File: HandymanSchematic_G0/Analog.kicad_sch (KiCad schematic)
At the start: 60 parts, among them Q1 BC847, Q2 BC847, U1 TL074, U2 TL074, U3 TL072

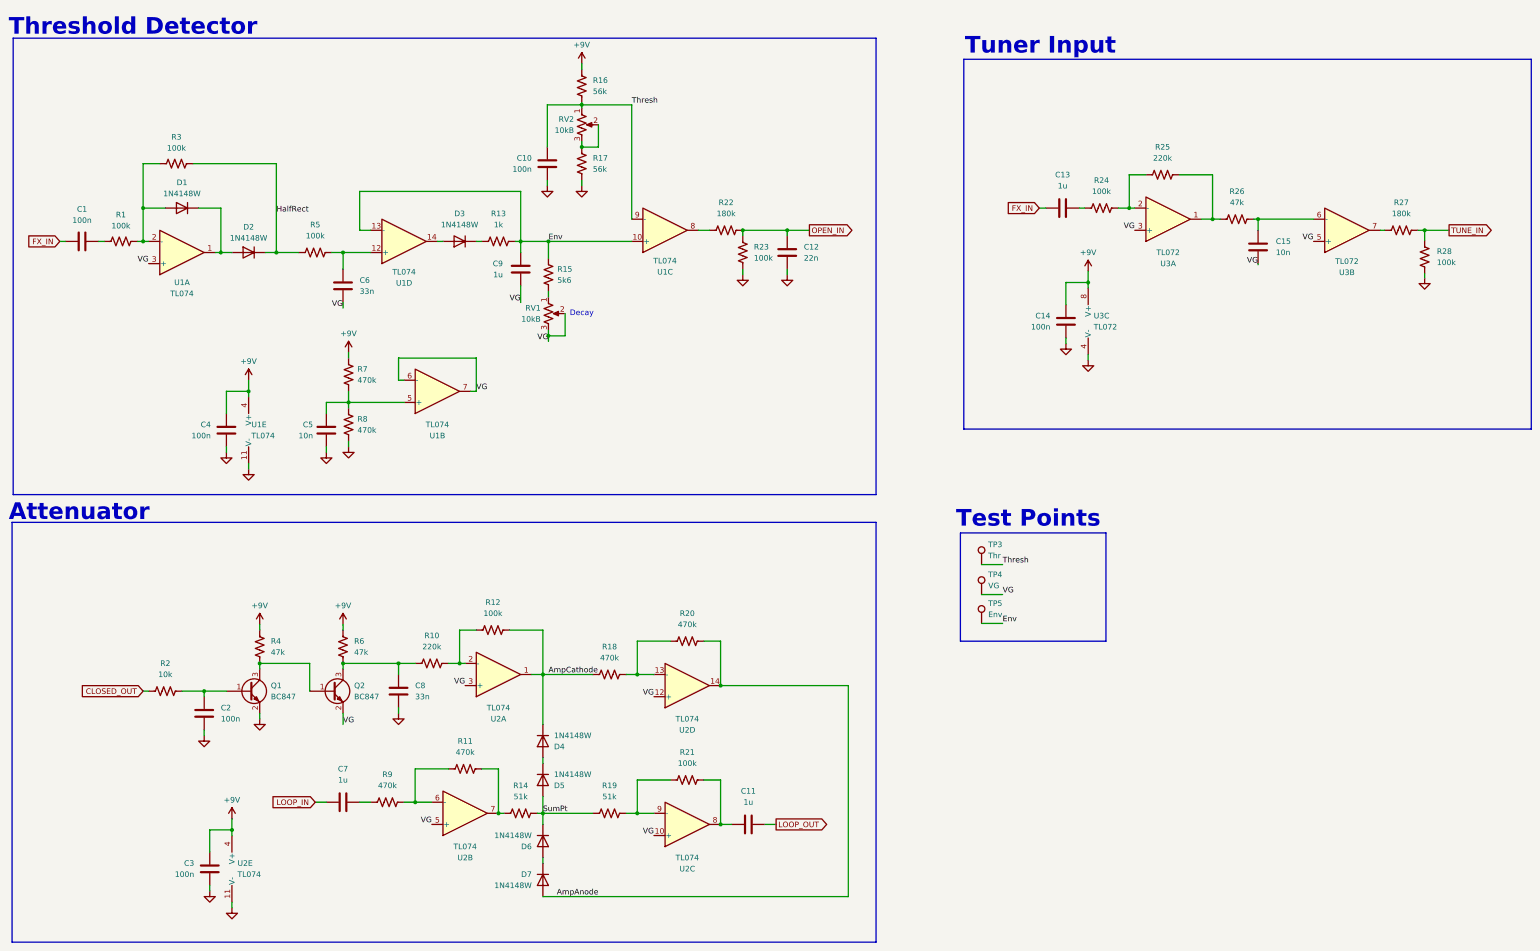
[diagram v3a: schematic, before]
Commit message: analog tweaks, 2 fewer op amps
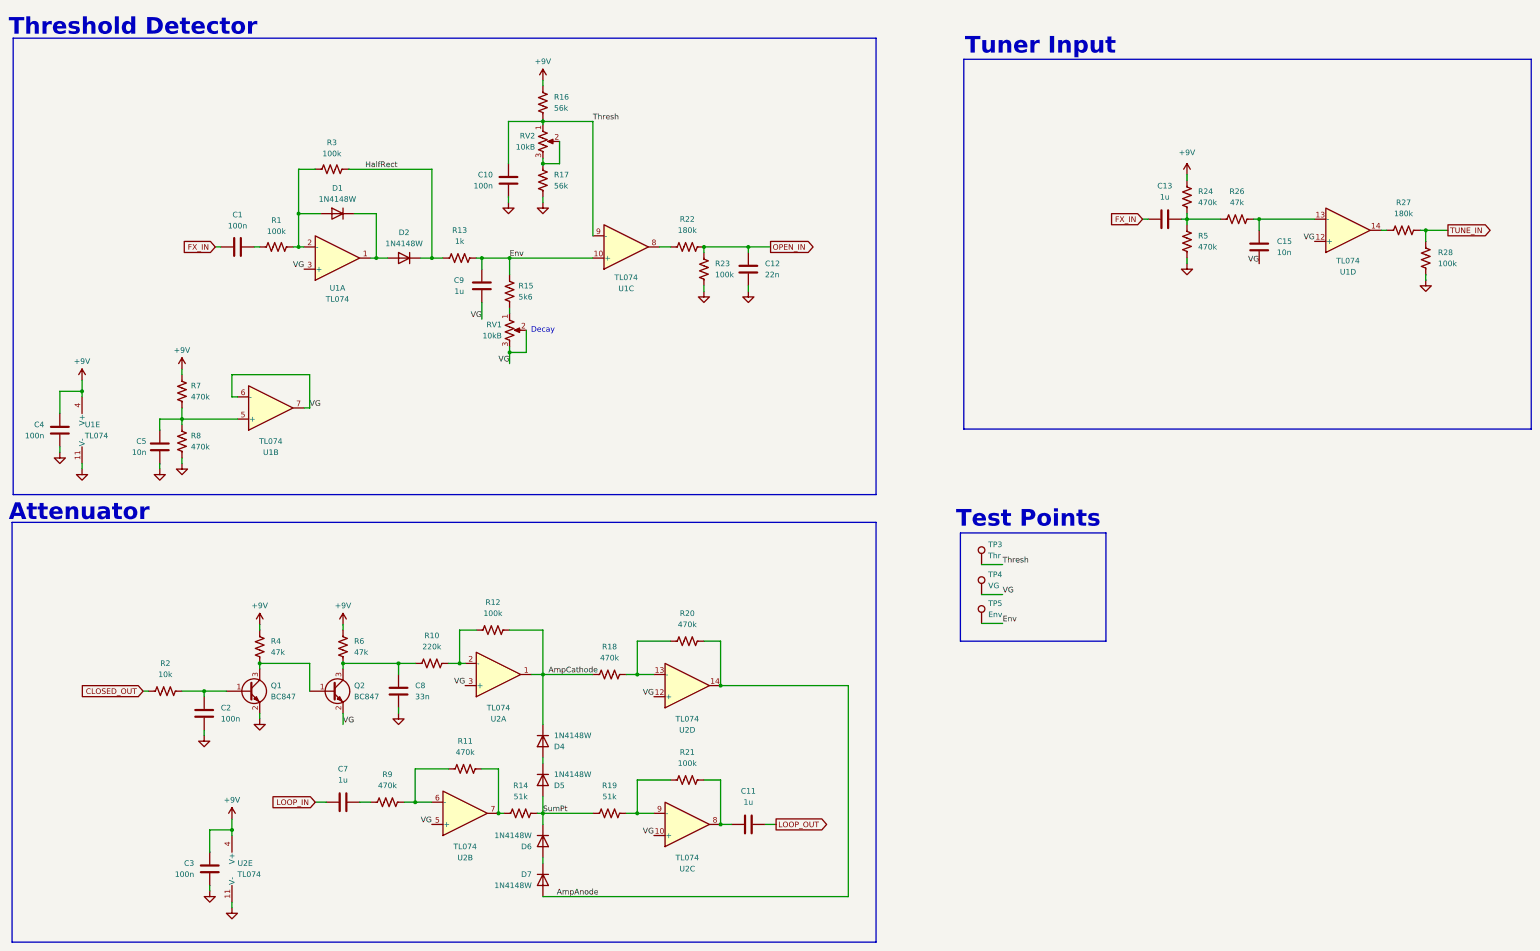
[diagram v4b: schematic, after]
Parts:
- removed C14: 100n, Capacitor_SMD:C_0805_2012Metric, symbol Device:C
- removed C6: 33n, Capacitor_SMD:C_0805_2012Metric, symbol Device:C
- removed D3: 1N4148W, Diode_SMD:D_SOD-123, symbol Diode:1N4148W
- removed R25: 220k, Resistor_SMD:R_0805_2012Metric, symbol Device:R_US
- removed U3: TL072, Package_SO:SOIC-8_3.9x4.9mm_P1.27mm, symbol Amplifier_Operational:TL072
- R24, R5: value 100k -> 470k
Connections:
- net +9V: now also R24.2
- net Env: no longer U1.13 (-)
- net GND: now also R5.1
- net HalfRect: now also R13.1; no longer R5.1
- net VG: now also U1.12 (+)
- net at U1.14: now also R27.1
- net at R5.2: now also C13.2, R24.1, R26.1; no longer U1.12 (+)
- net at C15.2, R26.2: now also U1.13 (-)
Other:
- moved on the sheet: C1, C10, C12, C13, C4, C5, C9, D1, D2, R1, R13, R15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

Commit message: simplified attenuator input stage
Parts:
- removed C8: 33n, Capacitor_SMD:C_0805_2012Metric, symbol Device:C
- removed Q2: BC847, Package_TO_SOT_SMD:SOT-23, symbol Transistor_BJT:BC847
- removed R6: 47k, Resistor_SMD:R_0805_2012Metric, symbol Device:R_US
- added D201: 1N4148W, Diode_SMD:D_SOD-123, symbol Diode:1N4148W
- added R201: 47k, Resistor_SMD:R_0805_2012Metric, symbol Device:R_US
- added R202: 100k, Resistor_SMD:R_0805_2012Metric, symbol Device:R_US
- R10: value 220k -> 47k
- R12: value 100k -> 470k
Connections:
- net VG: now also R202.2
- net at Q1.3 (C), R4.2: now also D201.2 (A)
- net at R10.1: now also R201.2, R202.1
- new net: D201.1 (K), R201.1
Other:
- moved on the sheet: C2, Q1, R2, R4

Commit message: prelim layout
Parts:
- removed TP4: VG, TestPoint:TestPoint_THTPad_D2.0mm_Drill1.0mm_VAL, symbol Connector:TestPoint
- renumbered C4 to C1, C11 to C10, C13 to C11, C15 to C12, C5 to C2, C2 to C4, C1 to C5, C7 to C6, C9 to C7, C10 to C8, C12 to C9, D201 to D1, D1 to D2, D2 to D3, R7 to R1, R13 to R11, R11 to R12, R12 to R13, R15 to R14, R14 to R15, R8 to R2, R22 to R20, R20 to R21, R21 to R22, R5 to R25, R2 to R3, R1 to R4, R4 to R5, R3 to R6, R201 to R7, R9 to R8, R202 to R9, TP3 to TP1, TP5 to TP3
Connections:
- net AmpAnode: now also U2.7; no longer U2.14
- net Env: now also U1.12 (+); no longer U1.10 (+)
- net Thresh: now also U1.13 (-); no longer U1.9 (-)
- net VG: now also U1.10 (+); no longer U1.12 (+)
- net at U1.8: now also R27.1; no longer R20.1
- net at U1.14: now also R20.1; no longer R27.1
- net at R18.2, R21.1: now also U2.6 (-); no longer U2.13 (-)
- net at R12.1, R8.2: now also U2.13 (-); no longer U2.6 (-)
- net at C12.2, R26.2: now also U1.9 (-); no longer U1.13 (-)
- net at R12.2, R15.1: now also U2.14; no longer U2.7
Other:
- moved on the sheet: U1C, U1D, U2B, U2D
